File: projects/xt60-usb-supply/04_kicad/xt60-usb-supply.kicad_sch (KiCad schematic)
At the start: 47 parts, among them J1 XT60PW-M, J2 USB-A, J3 USB-A, J4 USB-A, J5 TYPE-C-31-M-12A, Q1 AOD4185, U1 SY8368QNC, U2 SY8368QNC, U3 USBLC6-2SC6, U4 USBLC6-2SC6, U5 USBLC6-2SC6, U6 USBLC6-2SC6

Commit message: xt60-usb-supply: placement-stage DRC clean (0 violations, 0 parity); 39 airlines await routing
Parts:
- J2, J3, J4: symbol schwriter:USB-A_3f54c52f -> schwriter:USB-A_5ba19623
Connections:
- net GND: now also J2.SH (SHIELD), J3.SH (SHIELD), J4.SH (SHIELD); no longer J2.5 (SHIELD), J2.6 (SHIELD), J3.5 (SHIELD), J3.6 (SHIELD), J4.5 (SHIELD), J4.6 (SHIELD)
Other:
- moved on the sheet: J5, LED1, R1, R2, R3, R4, U3, U4, U5, U6

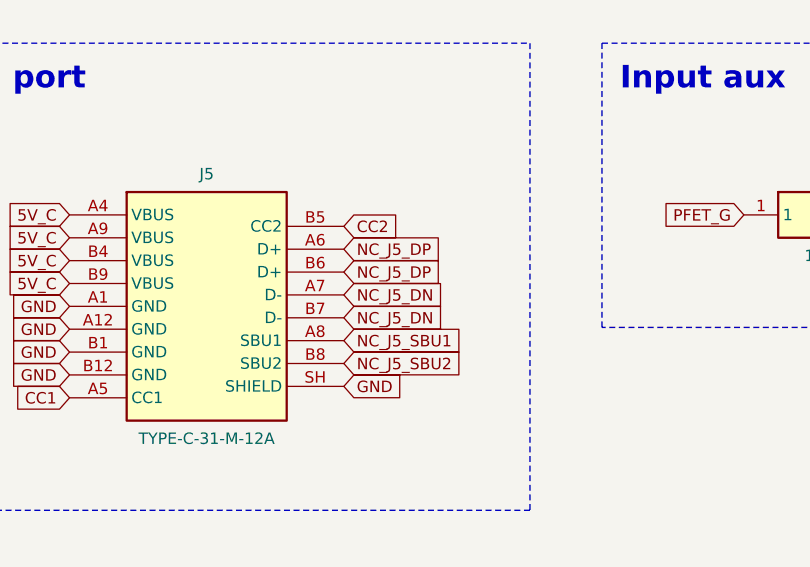
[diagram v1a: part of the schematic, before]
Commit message: xt60-usb-supply: 0 DRC violations placement stage; ILMT/EN taps + QFN thermal vias designed-in
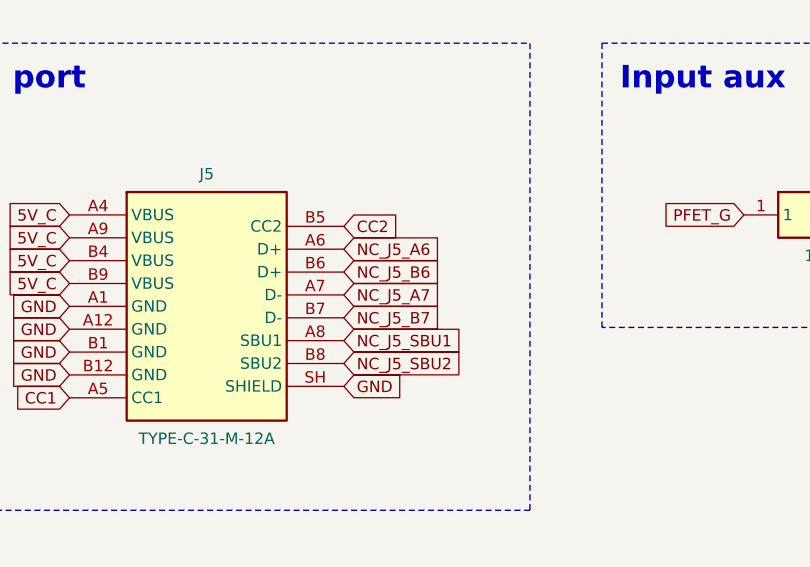
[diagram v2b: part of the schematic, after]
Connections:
- net NC_J5_DN renamed NC_J5_A7
- net NC_J5_A7: no longer J5.B7 (D-)
- net NC_J5_DP renamed NC_J5_A6
- net NC_J5_A6: no longer J5.B6 (D+)
- new net NC_J5_B6: J5.B6 (D+)
- new net NC_J5_B7: J5.B7 (D-)
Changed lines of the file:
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@@
     (property "Intersheetrefs" "${INTERSHEETREFS}" (at 381 153.67 0) (effects (font (size 1.27 1.27)) hide))
   )
-  (global_label "NC_J5_DP" (shape input) (at 381 156.21 0) (effects (font (size 1.27 1.27)) (justify left))
+  (global_label "NC_J5_A6" (shape input) (at 381 156.21 0) (effects (font (size 1.27 1.27)) (justify left))
     (property "Intersheetrefs" "${INTERSHEETREFS}" (at 381 156.21 0) (effects (font (size 1.27 1.27)) hide))
   )
-  (global_label "NC_J5_DP" (shape input) (at 381 158.75 0) (effects (font (size 1.27 1.27)) (justify left))
+  (global_label "NC_J5_B6" (shape input) (at 381 158.75 0) (effects (font (size 1.27 1.27)) (justify left))
     (property "Intersheetrefs" "${INTERSHEETREFS}" (at 381 158.75 0) (effects (font (size 1.27 1.27)) hide))
   )
-  (global_label "NC_J5_DN" (shape input) (at 381 161.29 0) (effects (font (size 1.27 1.27)) (justify left))
+  (global_label "NC_J5_A7" (shape input) (at 381 161.29 0) (effects (font (size 1.27 1.27)) (justify left))
     (property "Intersheetrefs" "${INTERSHEETREFS}" (at 381 161.29 0) (effects (font (size 1.27 1.27)) hide))
   )
-  (global_label "NC_J5_DN" (shape input) (at 381 163.83 0) (effects (font (size 1.27 1.27)) (justify left))
+  (global_label "NC_J5_B7" (shape input) (at 381 163.83 0) (effects (font (size 1.27 1.27)) (justify left))
     (property "Intersheetrefs" "${INTERSHEETREFS}" (at 381 163.83 0) (effects (font (size 1.27 1.27)) hide))
   )
